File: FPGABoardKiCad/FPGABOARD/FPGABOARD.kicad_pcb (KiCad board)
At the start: 4 copper layers, 78 x 51 mm, 80 parts, among them J1 USB_C_Receptacle_USB2.0_14P, J2 Program, J3 12PMOD, J4 6PMOD, J6 Conn_02x13_Odd_Even, SW1 ResetICE, SW2 BTN0, SW3 BTN1, SW4 BTN2, U1 AP2127K-1.2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

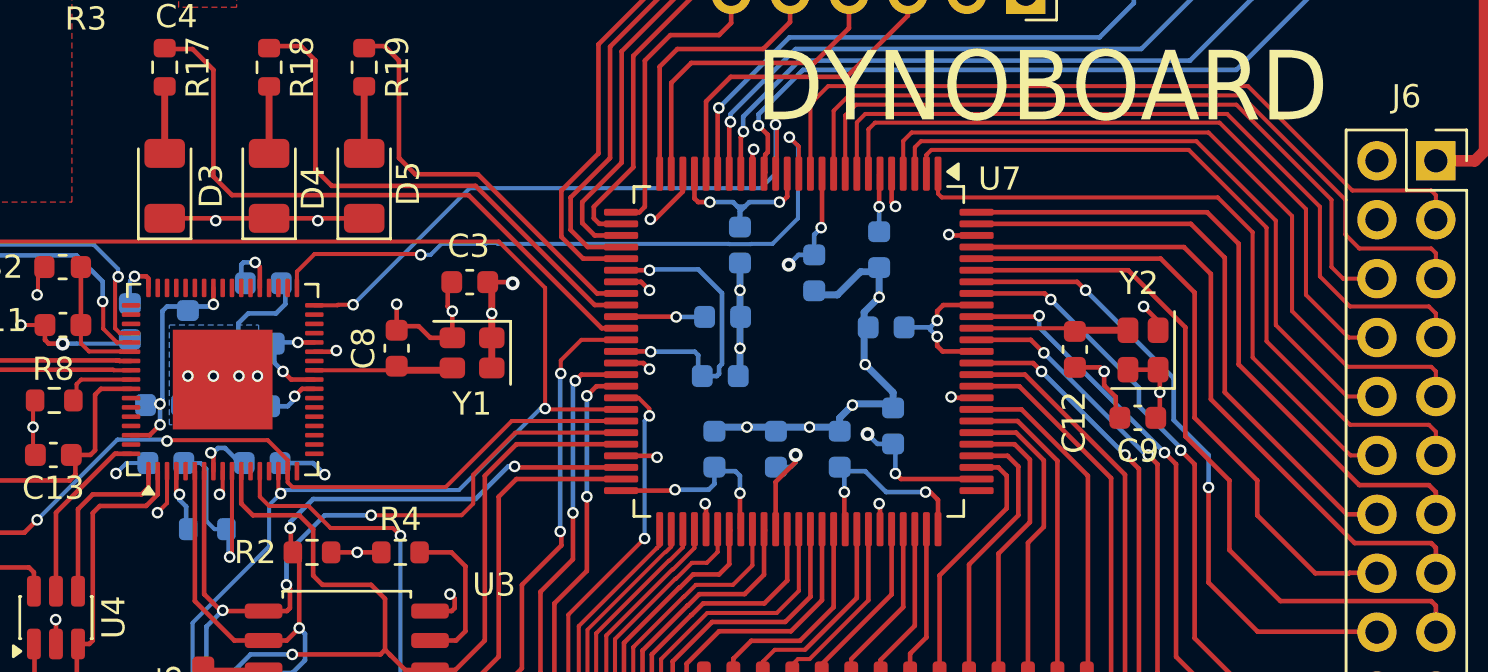
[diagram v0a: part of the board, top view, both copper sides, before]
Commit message: add bom
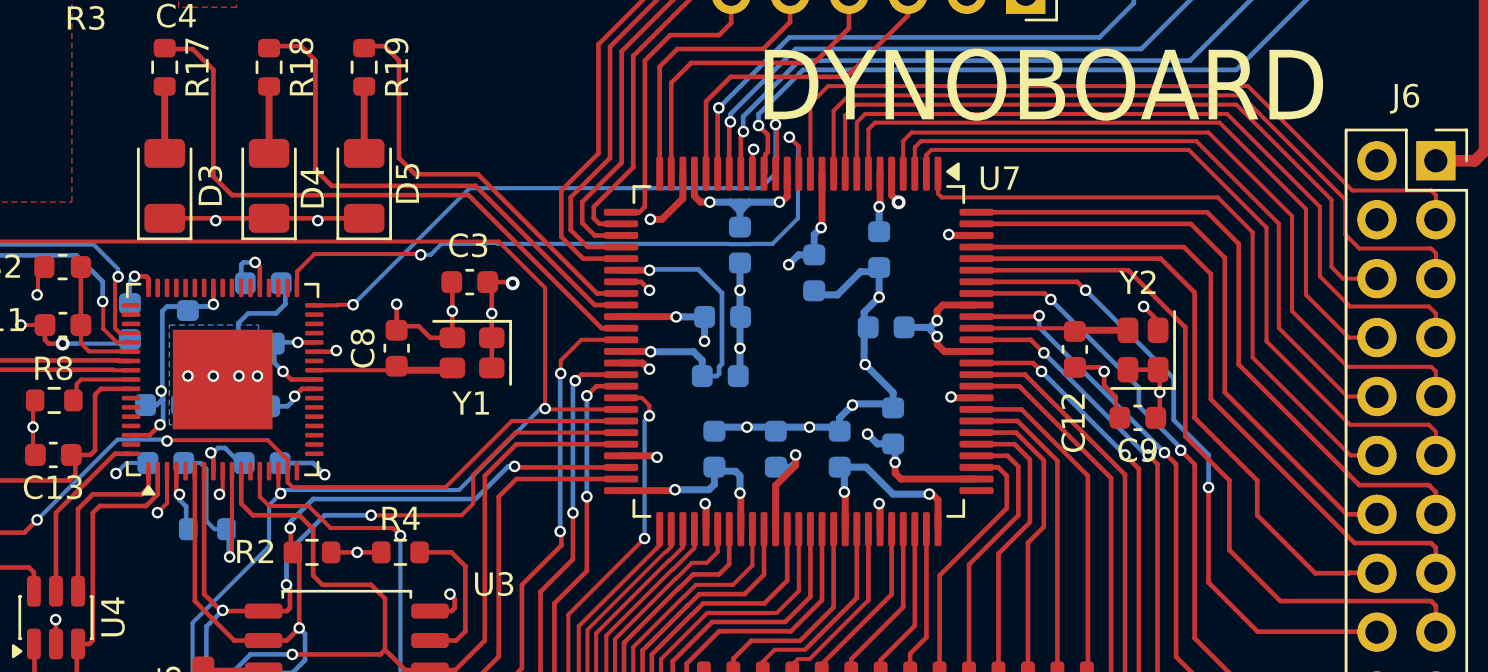
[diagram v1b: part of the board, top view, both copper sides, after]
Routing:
- net +1V2: track 33.7 -> 35.8 mm, vias 21 -> 22
- net +3V3: track 111.1 -> 112.1 mm
